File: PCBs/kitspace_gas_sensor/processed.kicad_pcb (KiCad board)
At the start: 2 copper layers, 45.5 x 32.5 mm, 15 parts, among them J1 Conn_01x04, U1 LM393

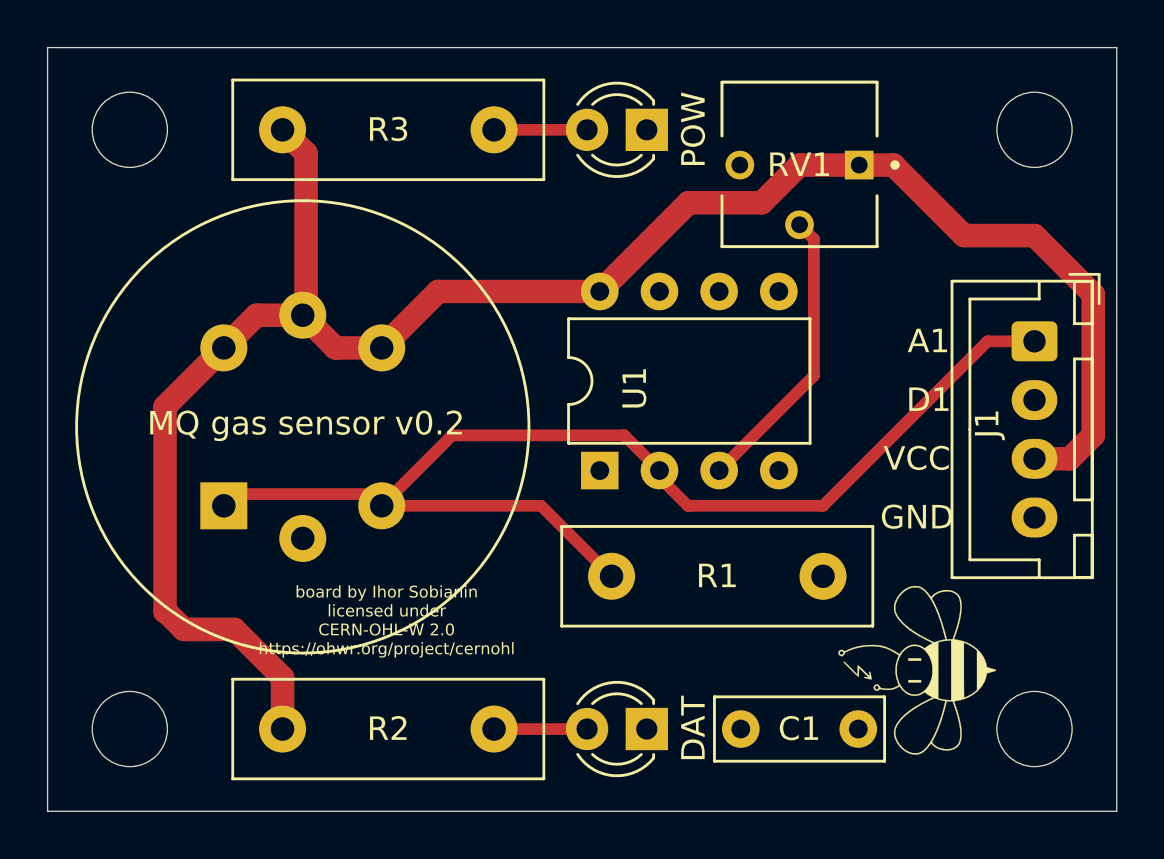
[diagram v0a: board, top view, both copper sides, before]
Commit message: recheck all circuits and clean up fill zone by rerouting the nets using freerouting and manually
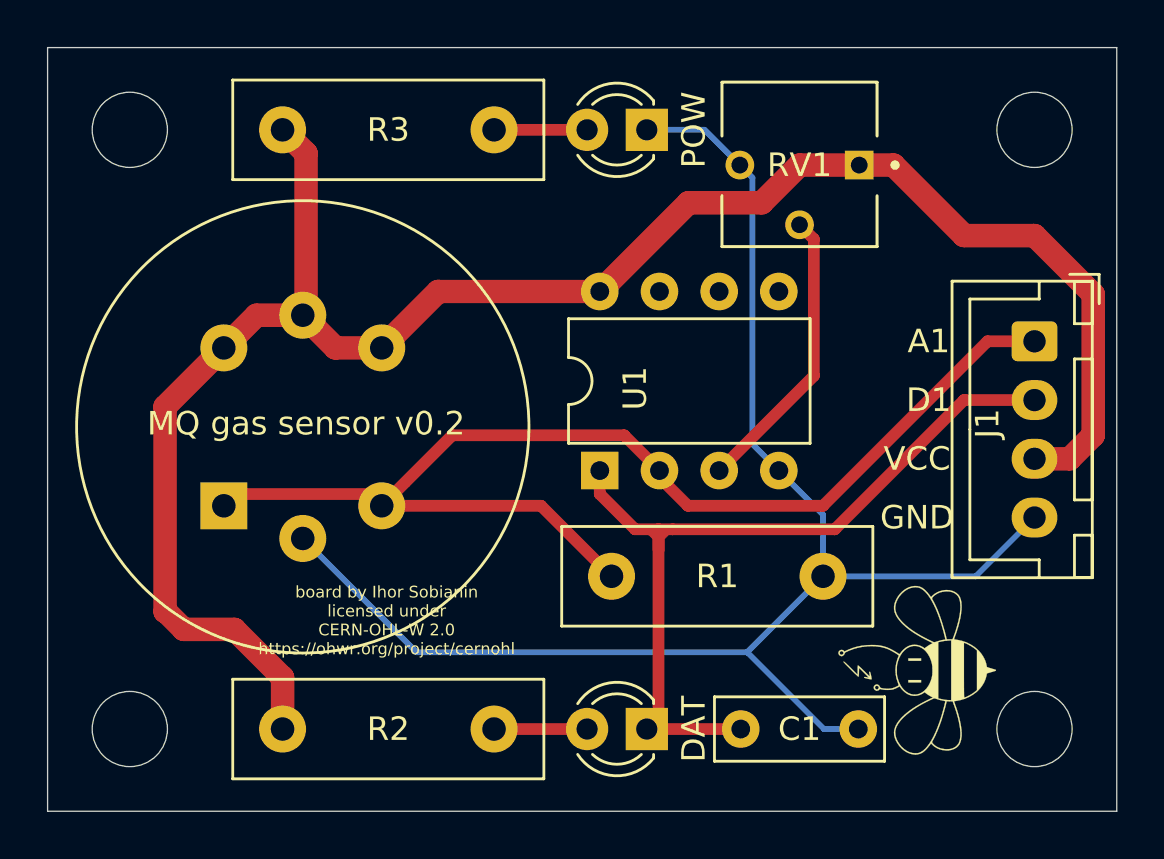
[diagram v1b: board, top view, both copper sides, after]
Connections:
- A1 pad 2: (no net) -> GND
- A1 pad 6: (no net) -> +5V
- C1 pad 1: (no net) -> D1
- C1 pad 2: (no net) -> GND
- D1 pad 1: (no net) -> D1
- D2 pad 1: (no net) -> GND
- J1 pad 2: (no net) -> D1
- J1 pad 4: (no net) -> GND
- R1 pad 2: (no net) -> GND
- RV1 pad 3: (no net) -> GND
- U1 pad 1: (no net) -> D1
- U1 pad 4: (no net) -> GND
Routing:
- net GND: track 0.00 -> 65.2 mm
- net D1: track 0.00 -> 37.4 mm

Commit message: clean psbc that are missed before
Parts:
- removed the REF** at (166.0, 116.0)
- removed the REF** at (127.5, 90.5)
- added REF**_2: MountingHole_3.2mm_M3_DIN965, MountingHole:MountingHole_3.2mm_M3_DIN965, F.Cu at (127.5, 90.5)
- added REF**_3: MountingHole_3.2mm_M3_DIN965, MountingHole:MountingHole_3.2mm_M3_DIN965, F.Cu at (166.0, 116.0)
- renumbered REF** to REF**_4
